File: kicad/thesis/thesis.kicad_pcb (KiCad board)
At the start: 2 copper layers, 85 x 60 mm, 14 parts, among them Q1 IRLZB8721, SW1 SW_DIP_x01, U1 INA219AxD

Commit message: naa wla na connect
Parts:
- moved Q1 5.37 mm to (111.5, 108.5)
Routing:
- net Net-(D1-A): track 85.4 -> 149.0 mm
- net Net-(D1-K): track 55.6 -> 104.9 mm
- net Net-(Q1-G): track 24.7 -> 28.8 mm
- net GND: track 202.6 -> 206.2 mm
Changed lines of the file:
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@@
 	(footprint "Package_TO_SOT_THT:TO-220-3_Vertical"
 		(layer "F.Cu")
-		(at 109.45 103.54 90)
+		(at 111.5 108.5 90)
 		(descr "TO-220-3, Vertical, RM 2.54mm, see https://www.vishay.com/docs/66542/to-220-1.pdf")
 		(tags "TO-220-3 Vertical RM 2.54mm")
@@
 	)
 	(segment
-		(start 131 116.5)
-		(end 131 96.2825)
+		(start 122.575 77.575)
+		(end 126 81)
+		(width 0.2)
+		(layer "F.Cu")
+		(net "Net-(D1-K)")
+	)
+	(segment
+		(start 130.5 82)
+		(end 130.5 92.5)
 		(width 0.2)
 		(layer "F.Cu")
@@
 	)
 	(segment
-		(start 119.955 94.58)
-		(end 113.7 88.325)
+		(start 113.7 77.8)
+		(end 113.7 77.575)
+		(width 0.2)
+		(layer "F.Cu")
+		(net "Net-(D1-K)")
+	)
+	(segment
+		(start 131 116.5)
+		(end 131 96.2825)
 		(width 0.2)
 		(layer "F.Cu")
@@
 	)
 	(segment
-		(start 128.1725 94.58)
-		(end 119.955 94.58)
+		(start 129.5 81)
+		(end 130.5 82)
+		(width 0.2)
+		(layer "F.Cu")
+		(net "Net-(D1-K)")
+	)
+	(segment
+		(start 130.5 92.5)
+		(end 128.42 94.58)
+		(width 0.2)
+		(layer "F.Cu")
+		(net "Net-(D1-K)")
+	)
+	(segment
+		(start 126 81)
+		(end 129.5 81)
+		(width 0.2)
+		(layer "F.Cu")
+		(net "Net-(D1-K)")
+	)
+	(segment
+		(start 113.7 77.575)
+		(end 122.575 77.575)
+		(width 0.2)
+		(layer "F.Cu")
+		(net "Net-(D1-K)")
+	)
+	(segment
+		(start 109 82.5)
+		(end 113.7 77.8)
+		(width 0.2)
+		(layer "F.Cu")
+		(net "Net-(D1-K)")
+	)
+	(segment
+		(start 100.31 82.5)
+		(end 109 82.5)
 		(width 0.2)
 		(layer "F.Cu")
@@
 	(segment
 		(start 113.7 88.325)
-		(end 113.7 77.575)
+		(end 113.7 92.2)
+		(width 0.2)
+		(layer "F.Cu")
+		(net "Net-(D1-K)")
+	)
+	(segment
+		(start 116.08 94.58)
+		(end 128.1725 94.58)
 		(width 0.2)
 		(layer "F.Cu")
@@
 	)
 	(segment
+		(start 93.31 75.5)
+		(end 100.31 82.5)
+		(width 0.2)
+		(layer "F.Cu")
+		(net "Net-(D1-K)")
+	)
+	(segment
+		(start 113.7 92.2)
+		(end 116.08 94.58)
+		(width 0.2)
+		(layer "F.Cu")
+		(net "Net-(D1-K)")
+	)
+	(segment
+		(start 128.42 94.58)
+		(end 128.1725 94.58)
+		(width 0.2)
+		(layer "F.Cu")
+		(net "Net-(D1-K)")
+	)
+	(segment
 		(start 128.1725 90.965)
 		(end 128.1725 83.045)
@@
 	)
 	(segment
-		(start 84 73)
-		(end 90.5 73)
+		(start 111.5 103.42)
+		(end 107.08 99)
 		(width 0.2)
 		(layer "F.Cu")
@@
 	)
 	(segment
-		(start 113.3625 125)
-		(end 135 125)
+		(start 84 73)
+		(end 90.5 73)
 		(width 0.2)
 		(layer "F.Cu")
@@
 	)
 	(segment
-		(start 135 125)
-		(end 137 123)
-		(width 0.2)
-		(layer "F.Cu")
-		(net "GND")
-	)
-	(segment
-		(start 108.91 99)
-		(end 109.45 98.46)
+		(start 137 73)
+		(end 135 71)
 		(width 0.2)
 		(layer "F.Cu")
@@
 	)
 	(segment
-		(start 111.535 123.1725)
-		(end 113.3625 125)
+		(start 110.96 103.96)
+		(end 111.5 103.42)
 		(width 0.2)
 		(layer "F.Cu")
@@
 	)
 	(segment
-		(start 137 73)
-		(end 135 71)
+		(start 82.5 74.5)
+		(end 84 73)
 		(width 0.2)
 		(layer "F.Cu")
@@
 	)
 	(segment
-		(start 82.5 74.5)
-		(end 84 73)
+		(start 112.3625 124)
+		(end 136 124)
 		(width 0.2)
 		(layer "F.Cu")
@@
 	)
 	(segment
-		(start 96.54 71)
-		(end 92.04 75.5)
+		(start 136 124)
+		(end 137 123)
 		(width 0.2)
 		(layer "F.Cu")
@@
 	)
 	(segment
-		(start 100.12 99)
-		(end 108.91 99)
+		(start 137 123)
+		(end 137 73)
 		(width 0.2)
 		(layer "F.Cu")
@@
 	)
 	(segment
-		(start 137 123)
-		(end 137 73)
+		(start 67.802 84.198)
+		(end 77.62 84.198)
 		(width 0.2)
 		(layer "F.Cu")
@@
 	)
 	(segment
-		(start 67.802 84.198)
-		(end 77.62 84.198)
+		(start 111.535 123.1725)
+		(end 112.3625 124)
 		(width 0.2)
 		(layer "F.Cu")
@@
 	)
 	(segment
+		(start 96.54 71)
+		(end 92.04 75.5)
+		(width 0.2)
+		(layer "F.Cu")
+		(net "GND")
+	)
+	(segment
+		(start 107.08 99)
+		(end 100.12 99)
+		(width 0.2)
+		(layer "F.Cu")
+		(net "GND")
+	)
+	(segment
 		(start 100.12 99)
 		(end 92.04 90.92)
@@
 	)
 	(segment
+		(start 110.5 108.5)
+		(end 103.5 101.5)
+		(width 0.2)
+		(layer "F.Cu")
+		(net "Net-(Q1-G)")
+	)
+	(segment
 		(start 92.5 103.81)
 		(end 92.69 104)
@@
 	(segment
 		(start 94.5 101.5)
-		(end 107.41 101.5)
+		(end 103.5 101.5)
 		(width 0.2)
 		(layer "F.Cu")
@@
 	)
 	(segment
-		(start 107.41 101.5)
-		(end 109.45 103.54)
+		(start 92.69 104)
+		(end 92.69 103.81)
 		(width 0.2)
 		(layer "F.Cu")
@@
 	)
 	(segment
-		(start 92.69 104)
-		(end 92.69 103.81)
+		(start 111.5 108.5)
+		(end 110.5 108.5)
 		(width 0.2)
 		(layer "F.Cu")
@@
 	)
 	(segment
+		(start 132 81.7925)
+		(end 132 120)
+		(width 0.2)
+		(layer "F.Cu")
+		(net "Net-(D1-A)")
+	)
+	(segment
 		(start 126.2075 101)
 		(end 128.1725 102.965)
@@
 	)
 	(segment
-		(start 109.45 101)
-		(end 117.5 101)
+		(start 130 122)
+		(end 125 122)
+		(width 0.2)
+		(layer "F.Cu")
+		(net "Net-(D1-A)")
+	)
+	(segment
+		(start 115.5 112.5)
+		(end 115.5 103)
+		(width 0.2)
+		(layer "F.Cu")
+		(net "Net-(D1-A)")
+	)
+	(segment
+		(start 132 120)
+		(end 130 122)
 		(width 0.2)
 		(layer "F.Cu")
@@
 	)
 	(segment
+		(start 125 122)
+		(end 115.5 112.5)
+		(width 0.2)
+		(layer "F.Cu")
+		(net "Net-(D1-A)")
+	)
+	(segment
 		(start 101 74.425)
 		(end 102.85 72.575)
@@
 	)
 	(segment
-		(start 101 88.325)
-		(end 101 77.575)
+		(start 111.5 105.96)
+		(end 112.54 105.96)
+		(width 0.2)
+		(layer "F.Cu")
+		(net "Net-(D1-A)")
+	)
+	(segment
+		(start 115.5 103)
+		(end 117.5 101)
+		(width 0.2)
+		(layer "F.Cu")
+		(net "Net-(D1-A)")
+	)
+	(segment
+		(start 112.54 105.96)
+		(end 115.5 103)
 		(width 0.2)
 		(layer "F.Cu")
@@
 		(width 0.2)
 		(layer "F.Cu")
+		(net "Net-(D1-A)")
+	)
+	(segment
+		(start 128.1725 77.965)
+		(end 132 81.7925)
+		(width 0.2)
+		(layer "F.Cu")

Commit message: Added track width changes
for accuracy
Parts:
- moved TH1 63.7 mm to (167.2, 103.9)
- moved A1 63.7 mm to (130.8, 101.8)
- moved L1 63.7 mm to (188.9, 75.3)
- moved L2 63.7 mm to (188.9, 100.1)
- moved L3 63.7 mm to (188.9, 88.8)
- moved L4 63.7 mm to (188.9, 63.8)
- moved Q1 63.7 mm to (172.2, 89.2)
- moved R1 63.7 mm to (147.8, 88.4)
- moved R2 63.7 mm to (153.2, 79.8)
- moved R3 63.7 mm to (153.4, 84.8)
- moved U1 63.7 mm to (146.4, 56.2)
- moved D1 63.7 mm to (174.4, 69.1)
- moved D2 63.7 mm to (174.4, 58.3)
- moved SW1 63.7 mm to (150.5, 105.2)

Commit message: Added Copper zone with GND
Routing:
- net +3.3V: track 118.1 -> 106.5 mm
- net Net-(A1-PadD9): track 47.2 -> 43.1 mm
- net Net-(L1-Pad2): track 7.92 -> 6.45 mm
- net GND: track 206.2 -> 206.8 mm, vias 0 -> 4
- added copper zone on B.Cu, net GND
- added copper zone on F.Cu, net GND

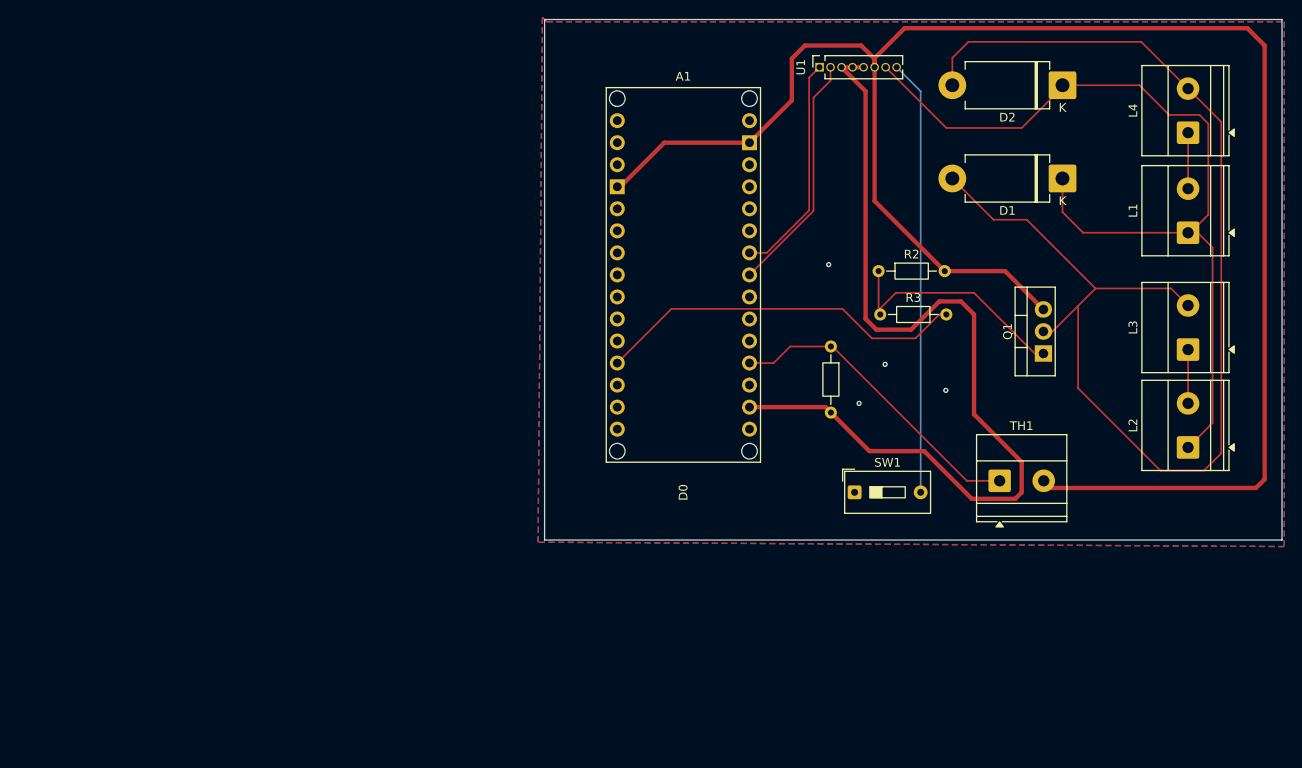
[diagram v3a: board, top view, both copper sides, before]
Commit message: Added new PCB Design
100x85mm new dimension, tried to isolate the transistor, need better track width
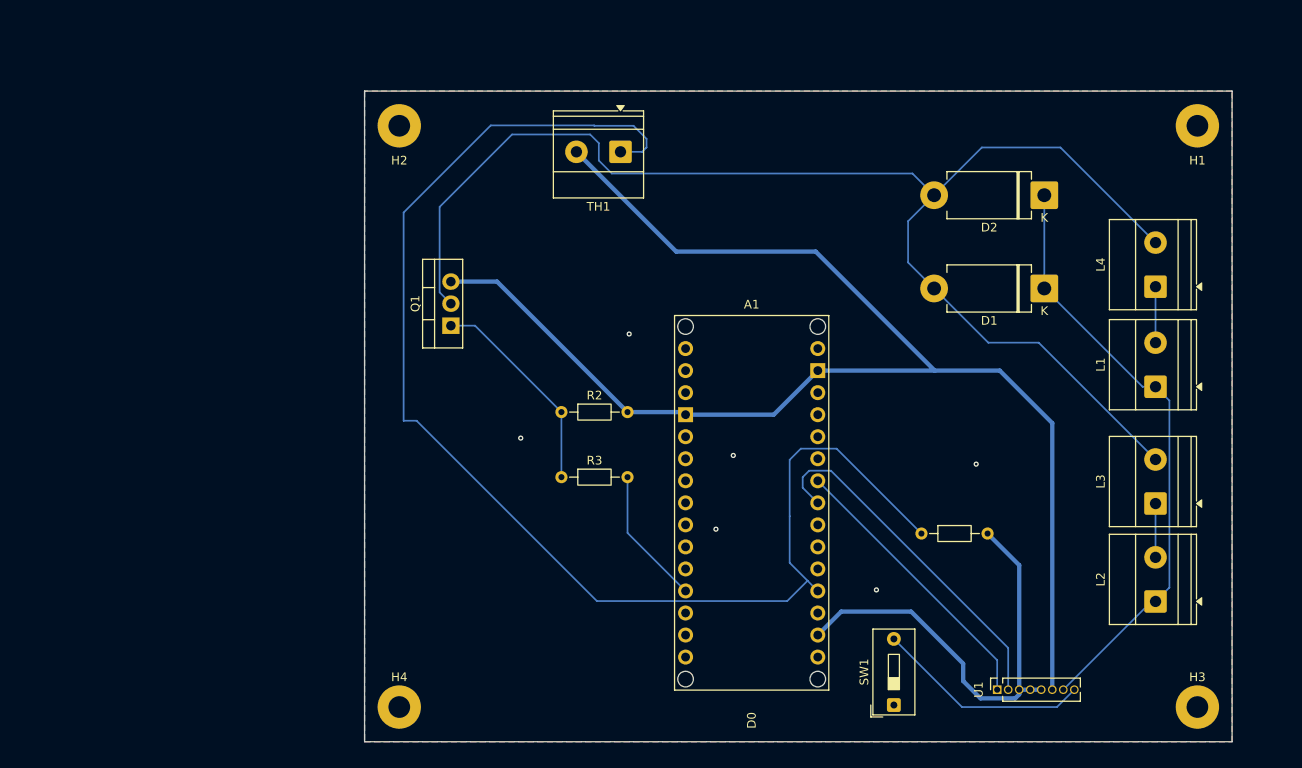
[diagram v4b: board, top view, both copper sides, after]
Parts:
- added H1: MountingHole_Pad, MountingHole:MountingHole_2.5mm_Pad, F.Cu at (190.0, 63.0)
- added H2: MountingHole_Pad, MountingHole:MountingHole_2.5mm_Pad, F.Cu at (98.0, 63.0)
- added H3: MountingHole_Pad, MountingHole:MountingHole_2.5mm_Pad, F.Cu at (190.0, 130.0)
- added H4: MountingHole_Pad, MountingHole:MountingHole_2.5mm_Pad, F.Cu at (98.0, 130.0)
- moved U1 74.6 mm to (166.9, 128.0)
- moved Q1 68.4 mm to (104.0, 86.0)
- moved TH1 57.9 mm to (123.5, 66.0), turned to 180 degrees
- moved R3 41.3 mm to (116.7, 103.5)
- moved R2 40.0 mm to (116.7, 96.0)
- moved A1 27.4 mm to (138.6, 128.1)
- moved SW1 24.9 mm to (155.0, 129.8), turned to 90 degrees
- moved R1 24.0 mm to (158.2, 110.0), turned to 0 degrees
- moved L1 18.1 mm to (185.2, 93.1)
- moved L2 18.1 mm to (185.2, 117.8)
- moved L3 18.1 mm to (185.2, 106.5)
- moved L4 18.1 mm to (185.2, 81.5)
- moved D1 12.8 mm to (172.3, 81.8)
- moved D2 12.8 mm to (172.3, 71.0)
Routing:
- net Net-(A1-PadA0): track 36.4 -> 153.4 mm
- net +3.3V: track 106.5 -> 52.4 mm
- net GND: track 206.8 -> 162.8 mm, vias 4 -> 0
- net Net-(D1-K): track 104.9 -> 69.2 mm, vias 0 -> 6
- net Net-(A1-PadD9): track 43.1 -> 15.9 mm
- net Net-(U1-IN+): track 50.1 -> 24.9 mm
- net /A0: track 27.8 -> 41.0 mm
- net Net-(D1-A): track 149.0 -> 156.4 mm
- net /A1: track 25.9 -> 32.6 mm
- net Net-(Q1-G): track 28.8 -> 24.4 mm
- added copper zone on B.Cu, net Net-(D1-K)
- added copper zone on F.Cu, net Net-(D1-K)
- removed copper zone on B.Cu, net GND
- removed copper zone on F.Cu, net GND
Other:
- board size 85 x 60 mm -> 100 x 75 mm

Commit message: Added Connector and thermistor
Track Width nlng
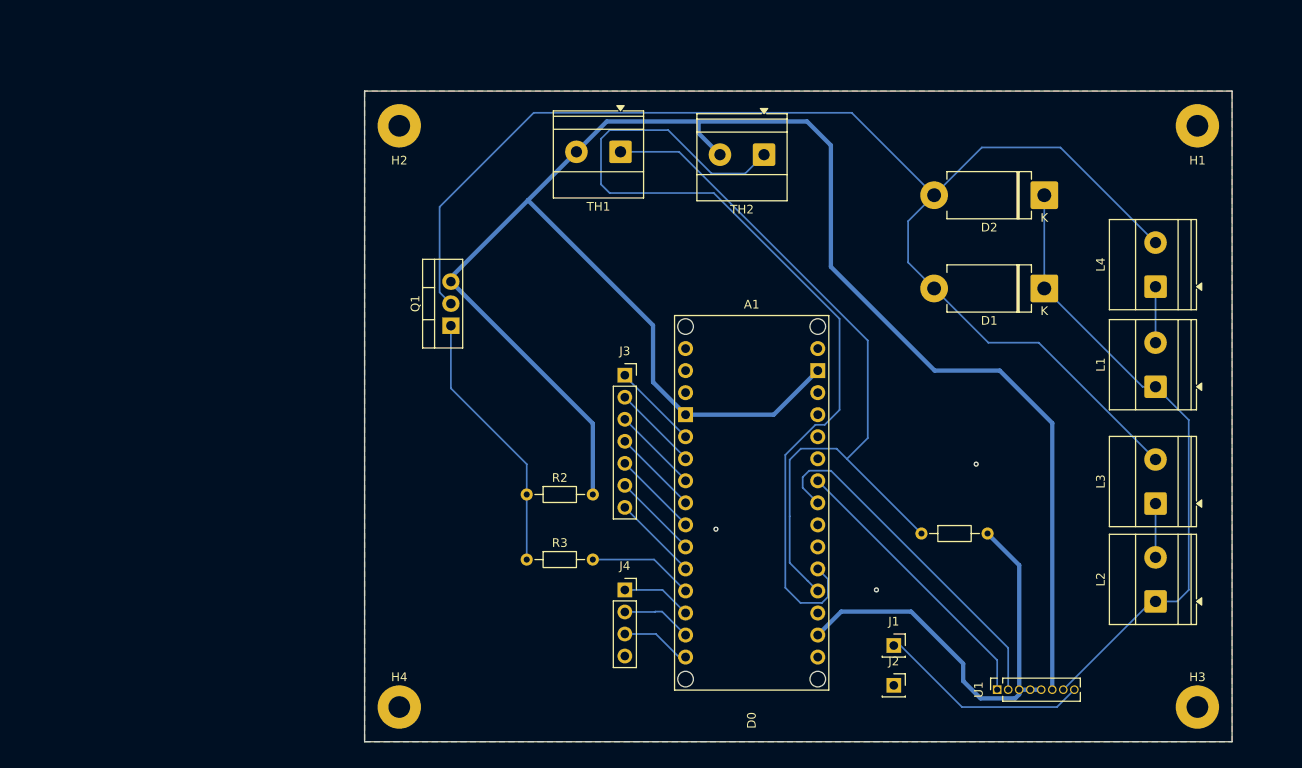
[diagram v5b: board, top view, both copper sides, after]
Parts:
- removed SW1: SW_DIP_x01, Button_Switch_THT:SW_DIP_SPSTx01_Slide_9.78x4.72mm_W7.62mm_P2.54mm
- added J1: Conn_01x01_Socket, Connector_PinSocket_2.54mm:PinSocket_1x01_P2.54mm_Vertical, F.Cu at (155.0, 122.9)
- added J2: Conn_01x01_Socket, Connector_PinSocket_2.54mm:PinSocket_1x01_P2.54mm_Vertical, F.Cu at (155.0, 127.5)
- added J3: Conn_01x07_Socket, Connector_PinSocket_2.54mm:PinSocket_1x07_P2.54mm_Vertical, F.Cu at (124.0, 91.8)
- added J4: Conn_01x04_Socket, Connector_PinSocket_2.54mm:PinSocket_1x04_P2.54mm_Vertical, F.Cu at (124.0, 116.5)
- added TH2: Thermistor_NTC, TerminalBlock_Phoenix:TerminalBlock_Phoenix_MKDS-1,5-2-5.08_1x02_P5.08mm_Horizontal, F.Cu at (140.0, 66.3)
- moved R2 10.3 mm to (112.7, 105.5)
- moved R3 10.3 mm to (112.7, 113.0)
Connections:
- A1 pad A1: unconnected-(A1-PadA1) -> Net-(A1-PadA1)
- A1 pad D10: unconnected-(A1-PadD10) -> Net-(J4-Pin_1)
- A1 pad D11: unconnected-(A1-D11_MOSI-PadD11) -> Net-(A1-D11_MOSI)
- A1 pad D12: unconnected-(A1-D12_MISO-PadD12) -> Net-(A1-D12_MISO)
- A1 pad D13: unconnected-(A1-D13_SCK-PadD13) -> Net-(A1-D13_SCK)
- A1 pad D2: unconnected-(A1-PadD2) -> Net-(J3-Pin_1)
- A1 pad D3: unconnected-(A1-PadD3) -> Net-(J3-Pin_2)
- A1 pad D4: unconnected-(A1-PadD4) -> Net-(J3-Pin_3)
- A1 pad D5: unconnected-(A1-PadD5) -> Net-(J3-Pin_4)
- A1 pad D6: unconnected-(A1-PadD6) -> Net-(J3-Pin_5)
- A1 pad D7: unconnected-(A1-PadD7) -> Net-(J3-Pin_6)
- A1 pad D8: unconnected-(A1-PadD8) -> Net-(J3-Pin_7)
- H1 pad 1: unconnected-(H1-Pad1) -> GND
- H2 pad 1: unconnected-(H2-Pad1) -> GND
- H3 pad 1: unconnected-(H3-Pad1) -> GND
- H4 pad 1: unconnected-(H4-Pad1) -> GND
- U1 pad 8: Net-(U1-IN+) -> Vin
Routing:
- net Net-(A1-PadA1): track 0.00 -> 105.2 mm
- net Net-(A1-PadA0): track 153.4 -> 88.4 mm
- net GND: track 162.8 -> 216.3 mm, vias 0 -> 3
- net Vin: track 0.00 -> 24.9 mm
- net Net-(U1-IN+): track 24.9 -> 0.00 mm
- net Net-(J3-Pin_3): track 0.00 -> 10.7 mm
- net Net-(J3-Pin_4): track 0.00 -> 10.6 mm
- net Net-(J3-Pin_7): track 0.00 -> 9.99 mm
- net Net-(J3-Pin_6): track 0.00 -> 9.99 mm
- net Net-(J3-Pin_5): track 0.00 -> 9.99 mm
- net Net-(J3-Pin_1): track 0.00 -> 9.99 mm
- net Net-(J3-Pin_2): track 0.00 -> 9.99 mm
- net Net-(A1-D11_MOSI): track 0.00 -> 8.13 mm
- net Net-(J4-Pin_1): track 0.00 -> 8.10 mm
- net Net-(A1-D12_MISO): track 0.00 -> 8.10 mm
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- added copper zone on B.Cu, net GND
- added copper zone on F.Cu, net GND
- removed copper zone on B.Cu, net Net-(D1-K)
- removed copper zone on F.Cu, net Net-(D1-K)

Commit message: Added Track Width
0.5 for GND and Power and 0.25 for net connections
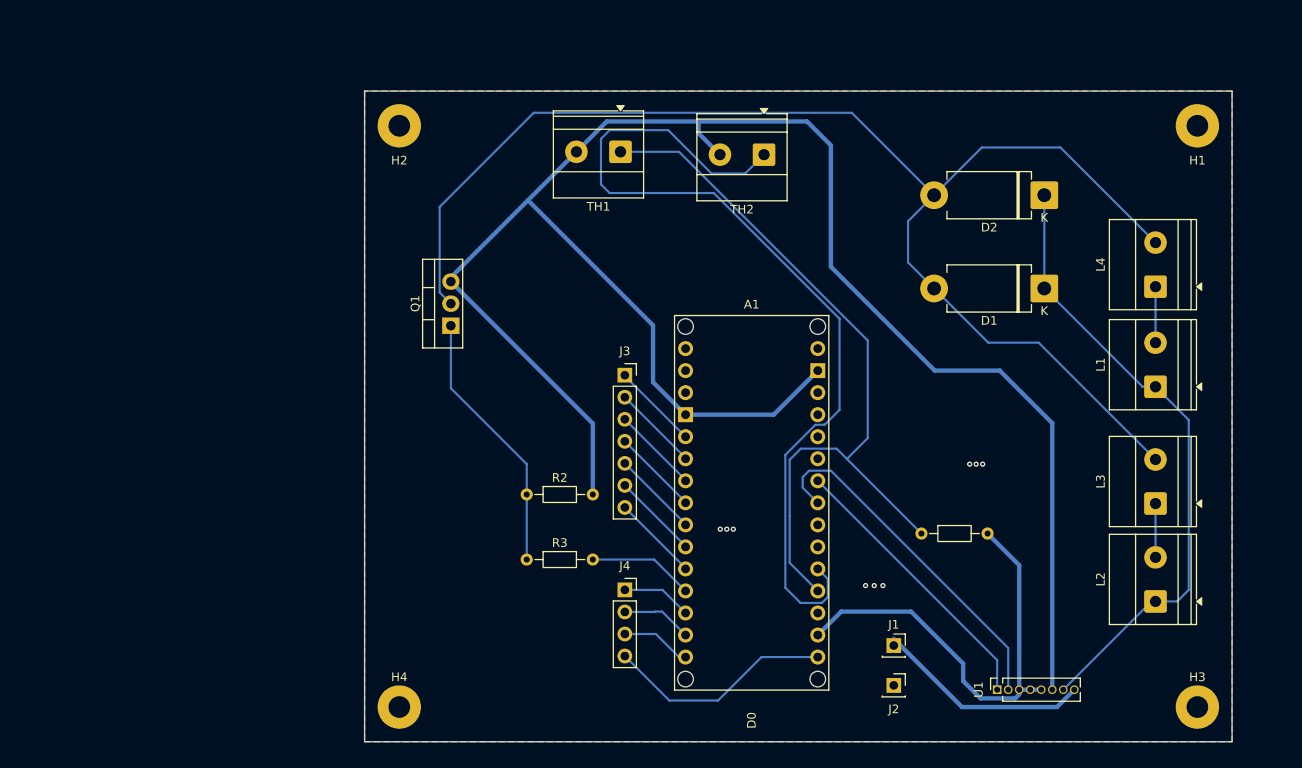
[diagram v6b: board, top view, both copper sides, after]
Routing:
- net Net-(A1-D13_SCK): track 0.00 -> 26.4 mm
- net GND: vias 3 -> 9

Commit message: Added labels
Added labels for pwr, gnd, and gnd
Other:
- board text added: "D10"
- board text added: "D11"
- board text added: "D12"
- board text added: "D13"
- board text added: "D2"
- board text added: "D3"
- board text added: "D4"
- board text added: "D5"
- board text added: "D6"
- board text added: "D7"
- board text added: "D8"
- board text added: "GND"
- board text added: "PWR"
